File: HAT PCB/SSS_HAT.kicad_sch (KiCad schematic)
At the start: 8 parts, among them J1 Conn_01x22_Socket, J2 Conn_01x22_Socket, J3 CAN1, J4 CAN2, U1 TJA1051T, U2 TJA1051T

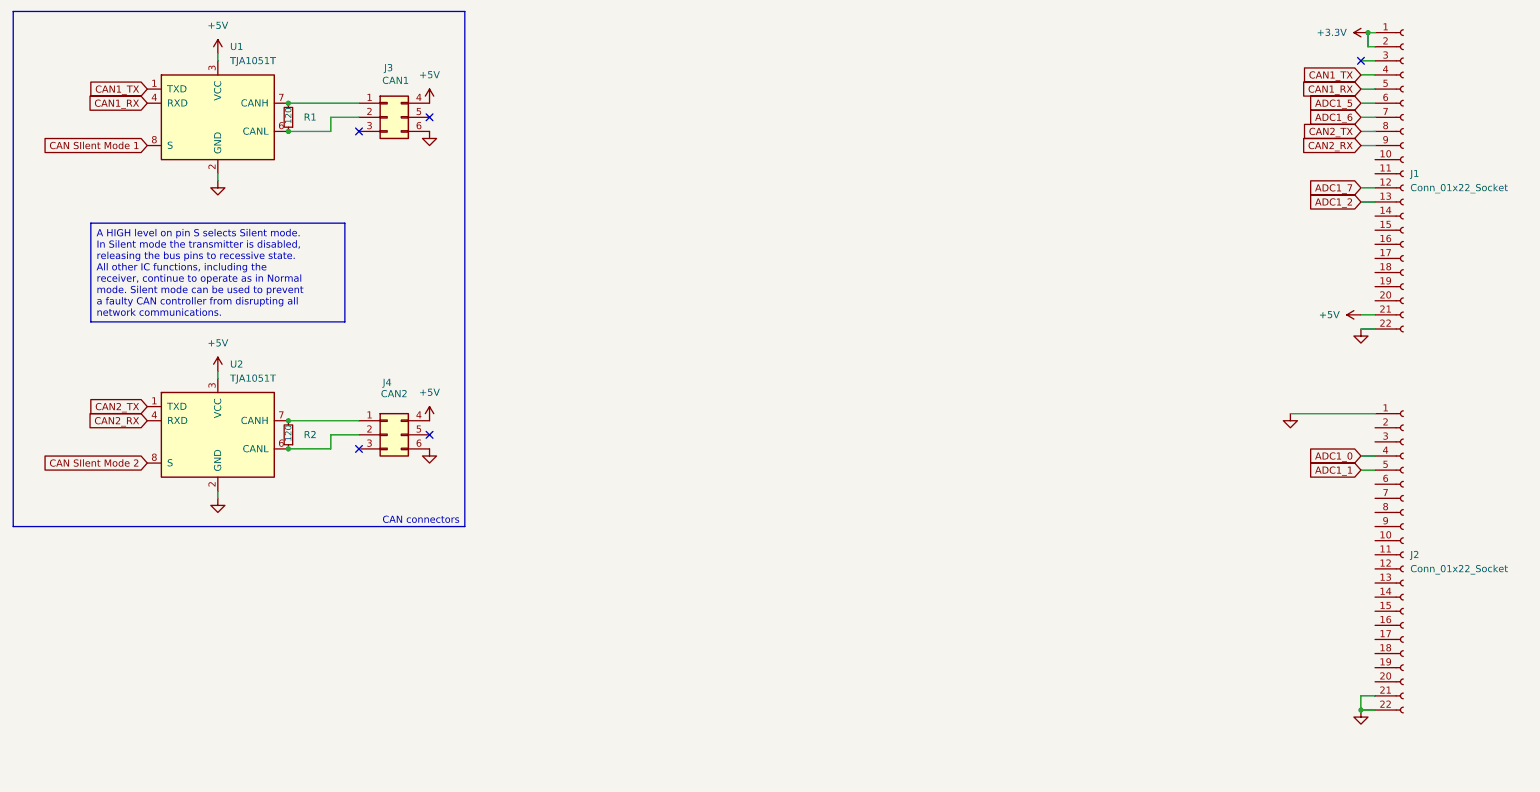
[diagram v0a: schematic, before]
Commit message: Added 2 CAN buses and 2 I2C buses
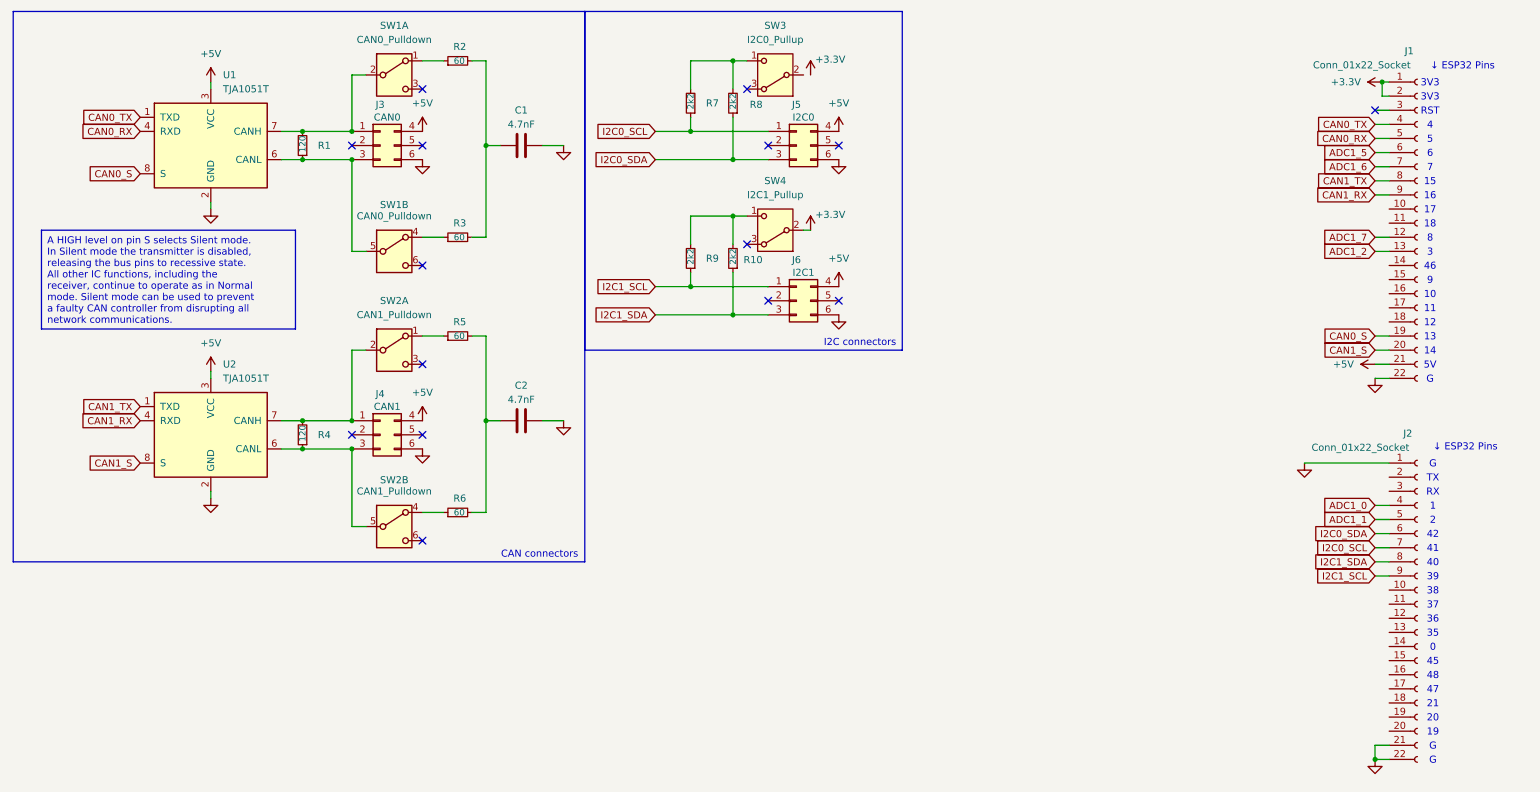
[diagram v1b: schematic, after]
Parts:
- added C1, C2: 4.7nF, Capacitor_SMD:C_0402_1005Metric_Pad0.74x0.62mm_HandSolder, symbol Device:C
- added J5: I2C0, Connector_Molex:Molex_Mega-Fit_76825-0006_2x03_P5.70mm_Horizontal, symbol Connector_Generic:Conn_02x03_Top_Bottom
- added J6: I2C1, Connector_Molex:Molex_Mega-Fit_76825-0006_2x03_P5.70mm_Horizontal, symbol Connector_Generic:Conn_02x03_Top_Bottom
- added R10, R7, R8, R9: 2k2, Resistor_SMD:R_0402_1005Metric_Pad0.72x0.64mm_HandSolder, symbol Device:R_Small
- added R2, R3, R5, R6: 60, Resistor_SMD:R_0402_1005Metric_Pad0.72x0.64mm_HandSolder, symbol Device:R_Small
- added SW1: CAN0_Pulldown, Button_Switch_SMD:SW_DPDT_CK_JS202011JCQN, symbol Switch:SW_DPDT_x2
- added SW2: CAN1_Pulldown, Button_Switch_SMD:SW_DPDT_CK_JS202011JCQN, symbol Switch:SW_DPDT_x2
- added SW3: I2C0_Pullup, Button_Switch_SMD:SW_DPDT_CK_JS202011JCQN, symbol Switch:SW_Nidec_CAS-120A1
- added SW4: I2C1_Pullup, Button_Switch_SMD:SW_DPDT_CK_JS202011JCQN, symbol Switch:SW_Nidec_CAS-120A1
- J3: value CAN1 -> CAN0; footprint NewMolexLibrary:Molex_MegaFit_2x03x5.70mm_Angled -> Connector_Molex:Molex_Mega-Fit_76825-0006_2x03_P5.70mm_Horizontal
- J4: value CAN2 -> CAN1; footprint NewMolexLibrary:Molex_MegaFit_2x03x5.70mm_Angled -> Connector_Molex:Molex_Mega-Fit_76825-0006_2x03_P5.70mm_Horizontal
- R1: footprint Resistor_SMD:R_0603_1608Metric_Pad0.98x0.95mm_HandSolder -> Resistor_SMD:R_0402_1005Metric_Pad0.72x0.64mm_HandSolder
- R4: renamed from R2; footprint Resistor_SMD:R_0603_1608Metric_Pad0.98x0.95mm_HandSolder -> Resistor_SMD:R_0402_1005Metric_Pad0.72x0.64mm_HandSolder
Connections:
- net CAN SIlent Mode 1 is gone; now on net CAN0_S: U1.8 (S)
- net CAN SIlent Mode 2 is gone; now on net CAN1_S: U2.8 (S)
- net CAN2_RX is gone; now on net CAN1_RX: J1.9 (Pin_9), U2.4 (RXD)
- net CAN2_TX is gone; now on net CAN1_TX: J1.8 (Pin_8), U2.1 (TXD)
- net +3.3V: now also SW4.2 (B)
- net +5V: now also J5.4 (Pin_4), J6.4 (Pin_4)
- net CAN1_RX: no longer J1.5 (Pin_5), U1.4 (RXD)
- net CAN1_TX: no longer J1.4 (Pin_4), U1.1 (TXD)
- net GND: now also C1.2, C2.2, J5.6 (Pin_6), J6.6 (Pin_6)
- net CAN0_S: now reaches J1.19 (Pin_19)
- net CAN1_S: now reaches J1.20 (Pin_20)
- net at R4.1, U2.6 (CANL): now also J4.3 (Pin_3), SW2.5 (B); no longer J4.2 (Pin_2)
- net at J4.1 (Pin_1), R4.2, U2.7 (CANH): now also SW2.2 (B)
- net at R1.1, U1.6 (CANL): now also J3.3 (Pin_3), SW1.5 (B); no longer J3.2 (Pin_2)
- net at J3.1 (Pin_1), R1.2, U1.7 (CANH): now also SW1.2 (B)
- net I2C0_SDA: now reaches J2.6 (Pin_6)
- net I2C0_SDA: now also J5.3 (Pin_3), R8.1
- net I2C0_SCL: now reaches J2.7 (Pin_7)
- net I2C0_SCL: now also J5.1 (Pin_1), R7.1
- net I2C1_SDA: now reaches J2.8 (Pin_8)
- net I2C1_SDA: now also J6.3 (Pin_3), R10.1
- net I2C1_SCL: now reaches J2.9 (Pin_9)
- net I2C1_SCL: now also J6.1 (Pin_1), R9.1
- new net: R10.2, R9.2, SW4.1 (C)
- new net: R2.1, SW1.1 (A)
- new net: R6.1, SW2.4 (A)
- new net: R5.1, SW2.1 (A)
- new net: C2.1, R5.2, R6.2
- new net: R3.1, SW1.4 (A)
- new net: C1.1, R2.2, R3.2
- new net: R7.2, R8.2, SW3.1 (C)
- new net CAN0_RX: J1.5 (Pin_5), U1.4 (RXD)
- new net CAN0_TX: J1.4 (Pin_4), U1.1 (TXD)
- no-connect marks 5 -> 15
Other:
- note added: "0"
- note added: "1"
- note added: "10"
- note added: "11"
- note added: "12"
- note added: "13"
- note added: "14"
- note added: "15"
- note added: "16"
- note added: "17"
- note added: "18"
- note added: "19"
- note added: "2"
- note added: "20"
- note added: "21"
- note added: "3"
- note added: "35"
- note added: "36"
- note added: "37"
- note added: "38"
- note added: "39"
- note added: "3V3"
- note added: "4"
- note added: "40"
- note added: "41"
- note added: "42"
- note added: "45"
- note added: "46"
- note added: "47"
- note added: "48"
- note added: "5"
- note added: "5V"
- note added: "6"
- note added: "7"
- note added: "8"
- note added: "9"
- note added: "G"
- note added: "I2C connectors"
- note added: "RST"
- note added: "RX"
- note added: "TX"
- note added: "↓ ESP32 Pins"
- moved on the sheet: J1, J2, J3, R1, R4, U1, U2

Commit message: Removed 1 I2C bus & 1 CAN transciever
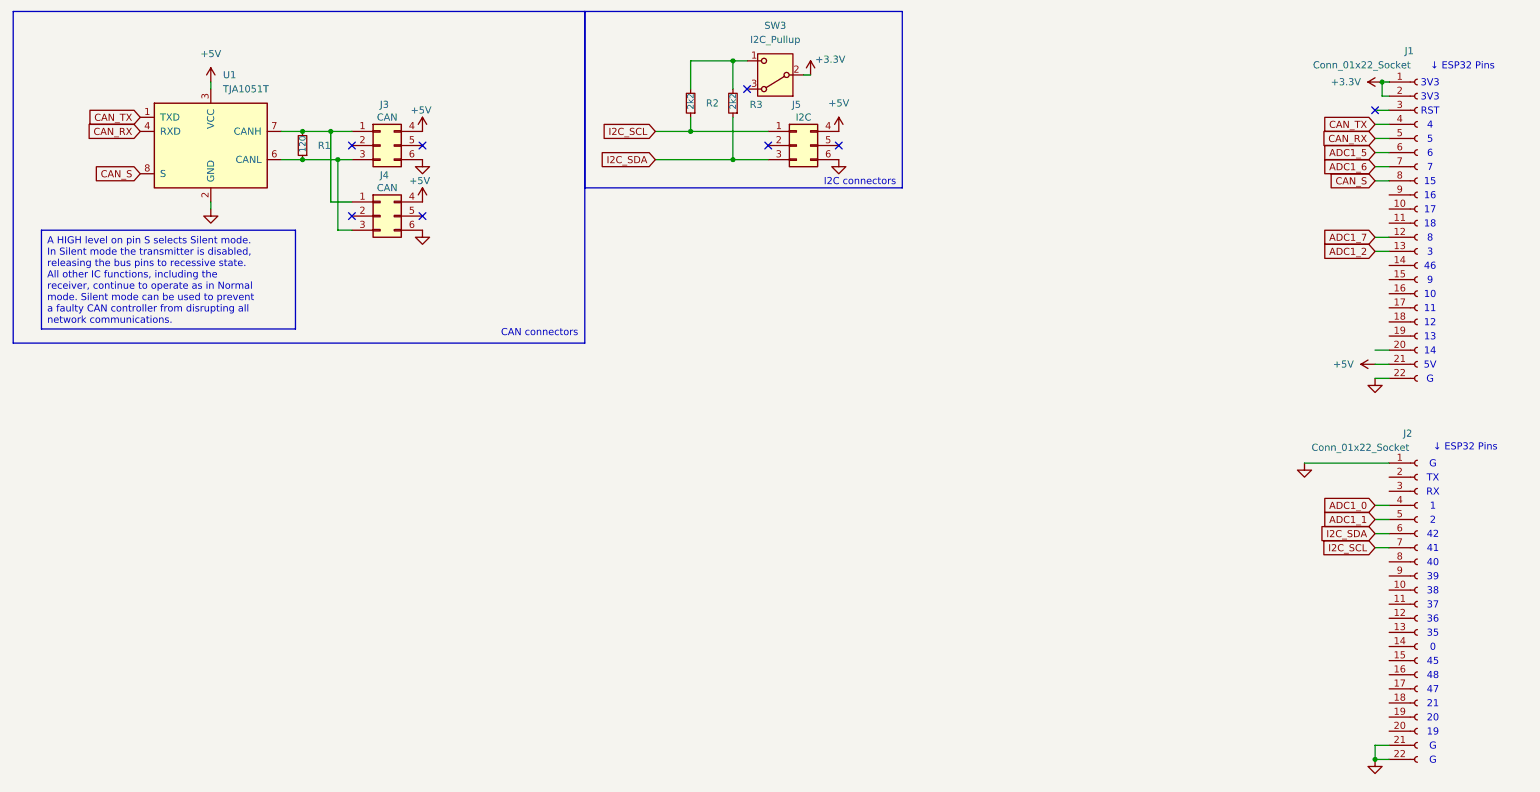
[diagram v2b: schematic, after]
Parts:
- removed C1, C2: 4.7nF, Capacitor_SMD:C_0402_1005Metric_Pad0.74x0.62mm_HandSolder, symbol Device:C
- removed J6: I2C1, Connector_Molex:Molex_Mega-Fit_76825-0006_2x03_P5.70mm_Horizontal, symbol Connector_Generic:Conn_02x03_Top_Bottom
- removed R10, R9: 2k2, Resistor_SMD:R_0402_1005Metric_Pad0.72x0.64mm_HandSolder, symbol Device:R_Small
- removed R2, R3, R5, R6: 60, Resistor_SMD:R_0402_1005Metric_Pad0.72x0.64mm_HandSolder, symbol Device:R_Small
- removed R4: 120, Resistor_SMD:R_0402_1005Metric_Pad0.72x0.64mm_HandSolder, symbol Device:R_Small
- removed SW1: CAN0_Pulldown, Button_Switch_SMD:SW_DPDT_CK_JS202011JCQN, symbol Switch:SW_DPDT_x2
- removed SW2: CAN1_Pulldown, Button_Switch_SMD:SW_DPDT_CK_JS202011JCQN, symbol Switch:SW_DPDT_x2
- removed SW4: I2C1_Pullup, Button_Switch_SMD:SW_DPDT_CK_JS202011JCQN, symbol Switch:SW_Nidec_CAS-120A1
- removed U2: TJA1051T, Package_SO:SOIC-8_3.9x4.9mm_P1.27mm, symbol Interface_CAN_LIN:TJA1051T
- J3: value CAN0 -> CAN
- J4: value CAN1 -> CAN
- J5: value I2C0 -> I2C
- SW3: value I2C0_Pullup -> I2C_Pullup
- renumbered R7 to R2, R8 to R3
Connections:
- net +3.3V: now also SW3.2 (B)
- net at J4.3 (Pin_3): now also J3.3 (Pin_3), R1.1, U1.6 (CANL)
- net at J4.1 (Pin_1): now also J3.1 (Pin_1), R1.2, U1.7 (CANH)
- net CAN0_RX renamed CAN_RX
- net CAN0_S: no longer names the net of J1.19 (Pin_19)
- net CAN0_S: no longer U1.8 (S)
- net CAN0_TX renamed CAN_TX
- net CAN1_RX: no longer names the net of J1.9 (Pin_9)
- net CAN1_S: no longer names the net of J1.20 (Pin_20)
- net CAN1_TX renamed CAN_S
- net CAN_S: now also U1.8 (S)
- net I2C0_SCL renamed I2C_SCL
- net I2C0_SDA renamed I2C_SDA
- net I2C1_SCL: no longer names the net of J2.9 (Pin_9)
- net I2C1_SDA: no longer names the net of J2.8 (Pin_8)
- no-connect marks 15 -> 8

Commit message: Added 2 Channel 18-bit ADC
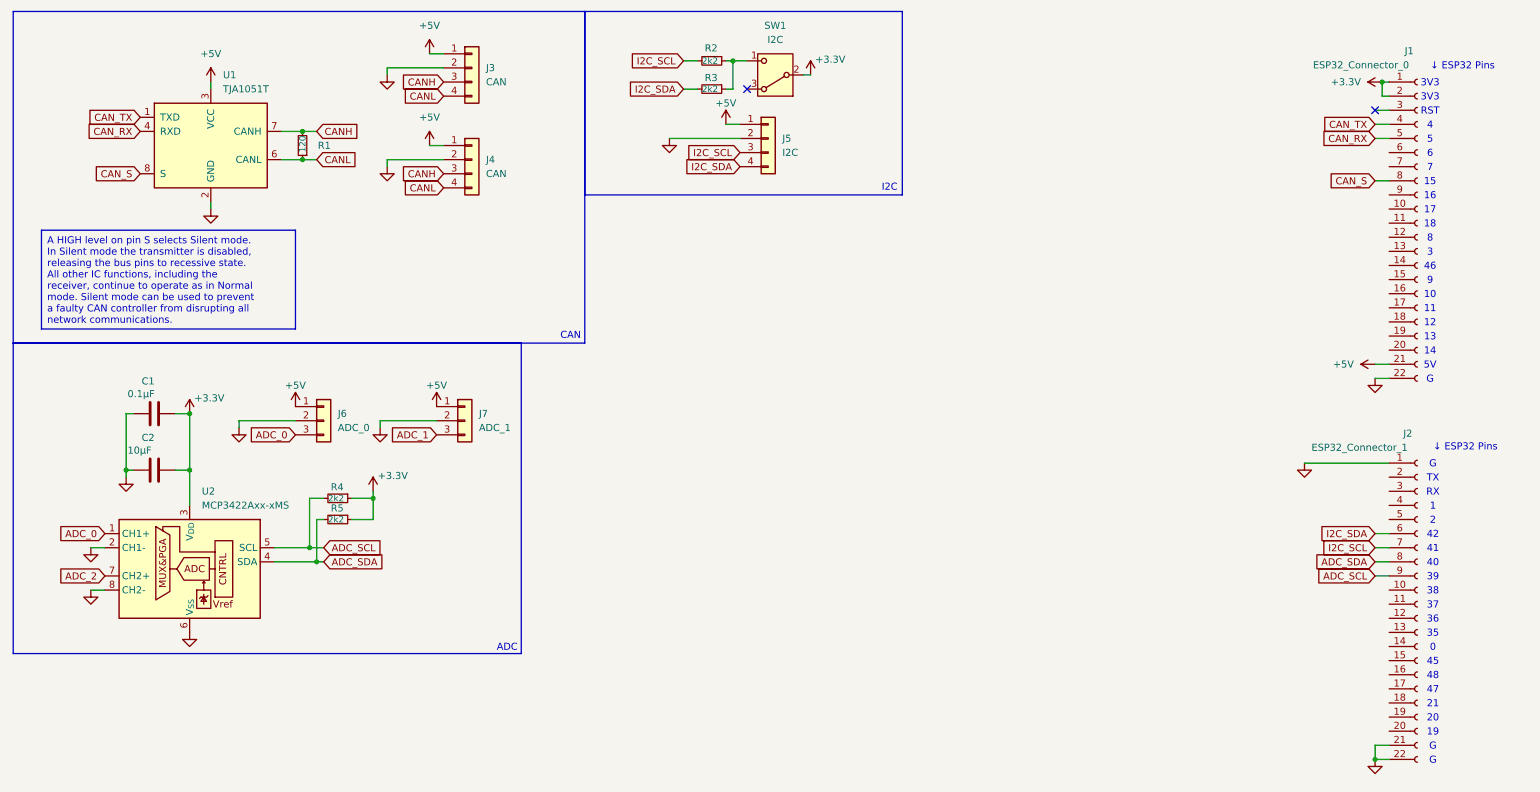
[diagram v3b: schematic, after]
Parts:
- removed J3, J4: CAN, Connector_Molex:Molex_Mega-Fit_76825-0006_2x03_P5.70mm_Horizontal, symbol Connector_Generic:Conn_02x03_Top_Bottom
- removed J5: I2C, Connector_Molex:Molex_Mega-Fit_76825-0006_2x03_P5.70mm_Horizontal, symbol Connector_Generic:Conn_02x03_Top_Bottom
- removed SW3: I2C_Pullup, Button_Switch_SMD:SW_DPDT_CK_JS202011JCQN, symbol Switch:SW_Nidec_CAS-120A1
- added C1: 0.1μF, Capacitor_SMD:C_0402_1005Metric_Pad0.74x0.62mm_HandSolder, symbol Device:C
- added C2: 10μF, Capacitor_SMD:C_0402_1005Metric_Pad0.74x0.62mm_HandSolder, symbol Device:C
- added J3, J4: CAN, Connector_Molex:Molex_Nano-Fit_105313-xx04_1x04_P2.50mm_Horizontal, symbol Connector_Generic:Conn_01x04
- added J5: I2C, Connector_Molex:Molex_Nano-Fit_105313-xx04_1x04_P2.50mm_Horizontal, symbol Connector_Generic:Conn_01x04
- added J6: ADC_0, Connector_Molex:Molex_Nano-Fit_105313-xx03_1x03_P2.50mm_Horizontal, symbol Connector_Generic:Conn_01x03
- added J7: ADC_1, Connector_Molex:Molex_Nano-Fit_105313-xx03_1x03_P2.50mm_Horizontal, symbol Connector_Generic:Conn_01x03
- added R4, R5: 2k2, Resistor_SMD:R_0402_1005Metric_Pad0.72x0.64mm_HandSolder, symbol Device:R_Small
- added SW1: I2C, Button_Switch_SMD:Nidec_Copal_CAS-120A, symbol Switch:SW_Nidec_CAS-120A1
- added U2: MCP3422Axx-xMS, Package_SO:MSOP-8_3x3mm_P0.65mm, symbol Analog_ADC:MCP3422Axx-xMS
- J1: value Conn_01x22_Socket -> ESP32_Connector_0; footprint Connector_PinSocket_1.27mm:PinSocket_1x22_P1.27mm_Vertical_SMD_Pin1Right -> Connector_PinSocket_1.27mm:PinSocket_1x22_P1.27mm_Vertical_SMD_Pin1Left
- J2: value Conn_01x22_Socket -> ESP32_Connector_1
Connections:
- net +3.3V: now also C1.1, C2.1, R4.1, R5.1, SW1.2 (B), U2.3 (V_{DD})
- net +5V: now also J3.1 (Pin_1), J4.1 (Pin_1), J5.1 (Pin_1), J6.1 (Pin_1), J7.1 (Pin_1)
- net GND: now also C1.2, C2.2, J3.2 (Pin_2), J4.2 (Pin_2), J5.2 (Pin_2), J6.2 (Pin_2), J7.2 (Pin_2), U2.2 (CH1-), U2.6 (V_{SS}), U2.8 (CH2-)
- net I2C_SCL: now also R2.2, J5.3 (Pin_3); no longer R2.1
- net I2C_SDA: now also R3.2, J5.4 (Pin_4); no longer R3.1
- net CANH: now reaches R1.2, U1.7 (CANH)
- net CANH: now also J3.3 (Pin_3), J4.3 (Pin_3)
- net CANL: now reaches R1.1, U1.6 (CANL)
- net CANL: now also J3.4 (Pin_4), J4.4 (Pin_4)
- net ADC_SDA: now reaches J2.8 (Pin_8)
- net ADC_SDA: now also R5.2, U2.4 (SDA)
- net ADC_SCL: now reaches J2.9 (Pin_9)
- net ADC_SCL: now also R4.2, U2.5 (SCL)
- net ADC1_0: no longer names the net of J2.4 (Pin_4)
- net ADC1_1: no longer names the net of J2.5 (Pin_5)
- net ADC1_2: no longer names the net of J1.13 (Pin_13)
- net ADC1_5: no longer names the net of J1.6 (Pin_6)
- net ADC1_6: no longer names the net of J1.7 (Pin_7)
- net ADC1_7: no longer names the net of J1.12 (Pin_12)
- new net: R2.1, R3.1, SW1.1 (C)
- new net ADC_0: J6.3 (Pin_3), U2.1 (CH1+)
- new net ADC_1: J7.3 (Pin_3)
- new net ADC_2: U2.7 (CH2+)
- no-connect marks 8 -> 2
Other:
- note added: "ADC"
- note added: "CAN"
- note added: "I2C"
- note removed: "CAN connectors"
- note removed: "I2C connectors"
- moved on the sheet: R2, R3

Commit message: added IMU
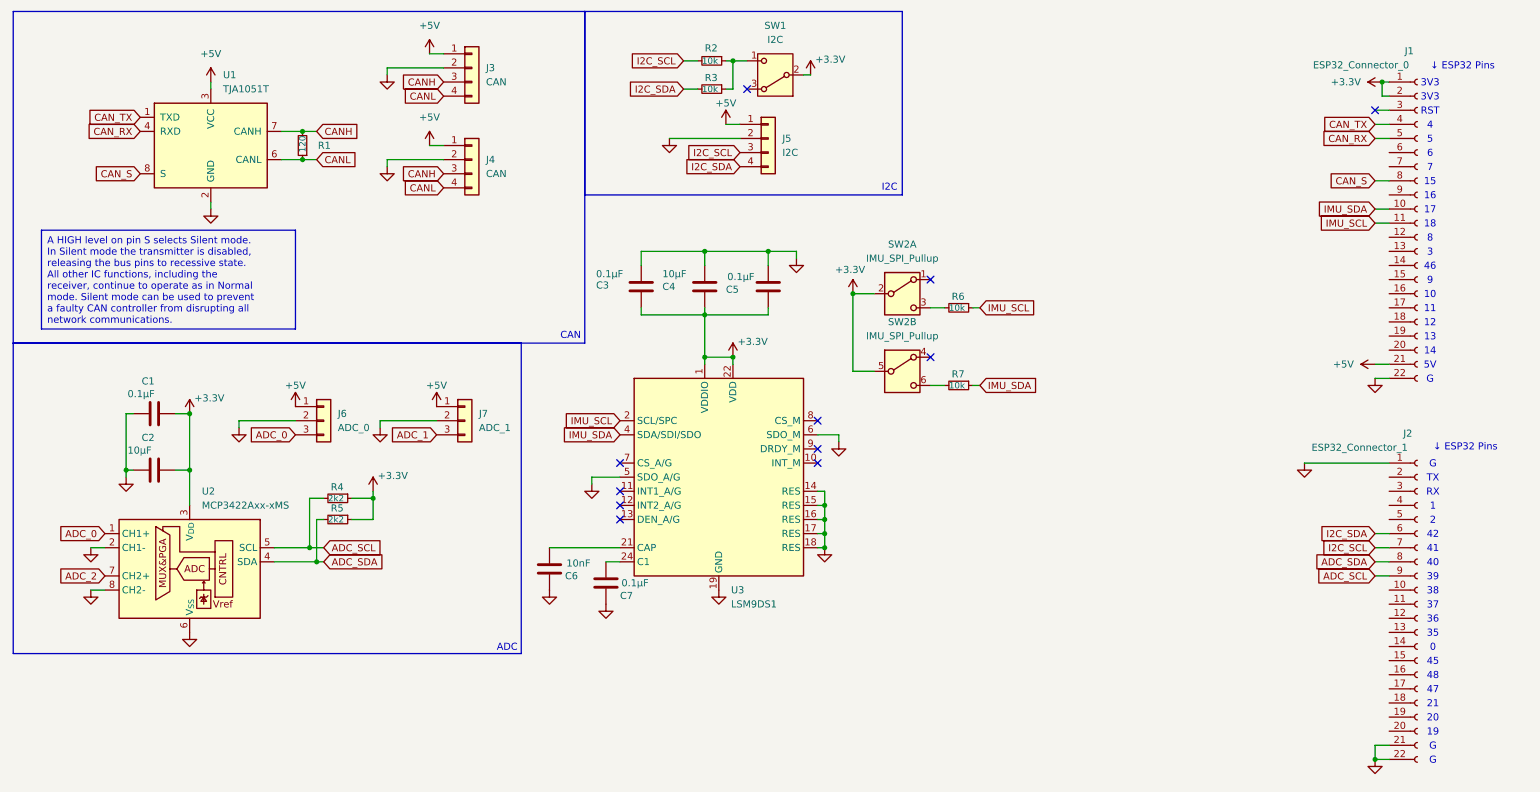
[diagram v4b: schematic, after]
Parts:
- added C3, C5, C7: 0.1μF, Capacitor_SMD:C_0402_1005Metric_Pad0.74x0.62mm_HandSolder, symbol Device:C
- added C4: 10μF, Capacitor_SMD:C_0402_1005Metric_Pad0.74x0.62mm_HandSolder, symbol Device:C
- added C6: 10nF, Capacitor_SMD:C_0402_1005Metric_Pad0.74x0.62mm_HandSolder, symbol Device:C
- added R6, R7: 10k, Resistor_SMD:R_0402_1005Metric_Pad0.72x0.64mm_HandSolder, symbol Device:R_Small
- added SW2: IMU_SPI_Pullup, Button_Switch_SMD:SW_DPDT_CK_JS202011JCQN, symbol Switch:SW_DPDT_x2
- added U3: LSM9DS1, Package_LGA:LGA-24L_3x3.5mm_P0.43mm, symbol Sensor_Motion:LSM9DS1
- R2, R3: value 2k2 -> 10k
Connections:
- net +3.3V: now also C3.2, C4.2, C5.2, SW2.2 (B), SW2.5 (B), U3.1 (VDDIO), U3.22 (VDD), U3.23 (VDD), U3.3 (VDDIO)
- net GND: now also C3.1, C4.1, C5.1, C6.2, C7.2, U3.14 (RES), U3.15 (RES), U3.16 (RES), U3.17 (RES), U3.18 (RES), U3.19 (GND), U3.20 (GND), U3.5 (SDO_A/G), U3.6 (SDO_M)
- net IMU_SDA: now reaches J1.10 (Pin_10)
- net IMU_SDA: now also R7.1, U3.4 (SDA/SDI/SDO)
- net IMU_SCL: now reaches J1.11 (Pin_11)
- net IMU_SCL: now also R6.1, U3.2 (SCL/SPC)
- new net: R6.2, SW2.3 (C)
- new net: C7.1, U3.24 (C1)
- new net: R7.2, SW2.6 (C)
- new net: C6.1, U3.21 (CAP)
- no-connect marks 2 -> 11
